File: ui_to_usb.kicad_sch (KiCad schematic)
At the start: 30 parts, among them J1 PM254-2-06-S-8.5, J2 TYPE-C-31-M-12, U3 USBLC6-2SC6, U4 CH32V305GBU6, U6 SPX3819M5-L, Y2 8M

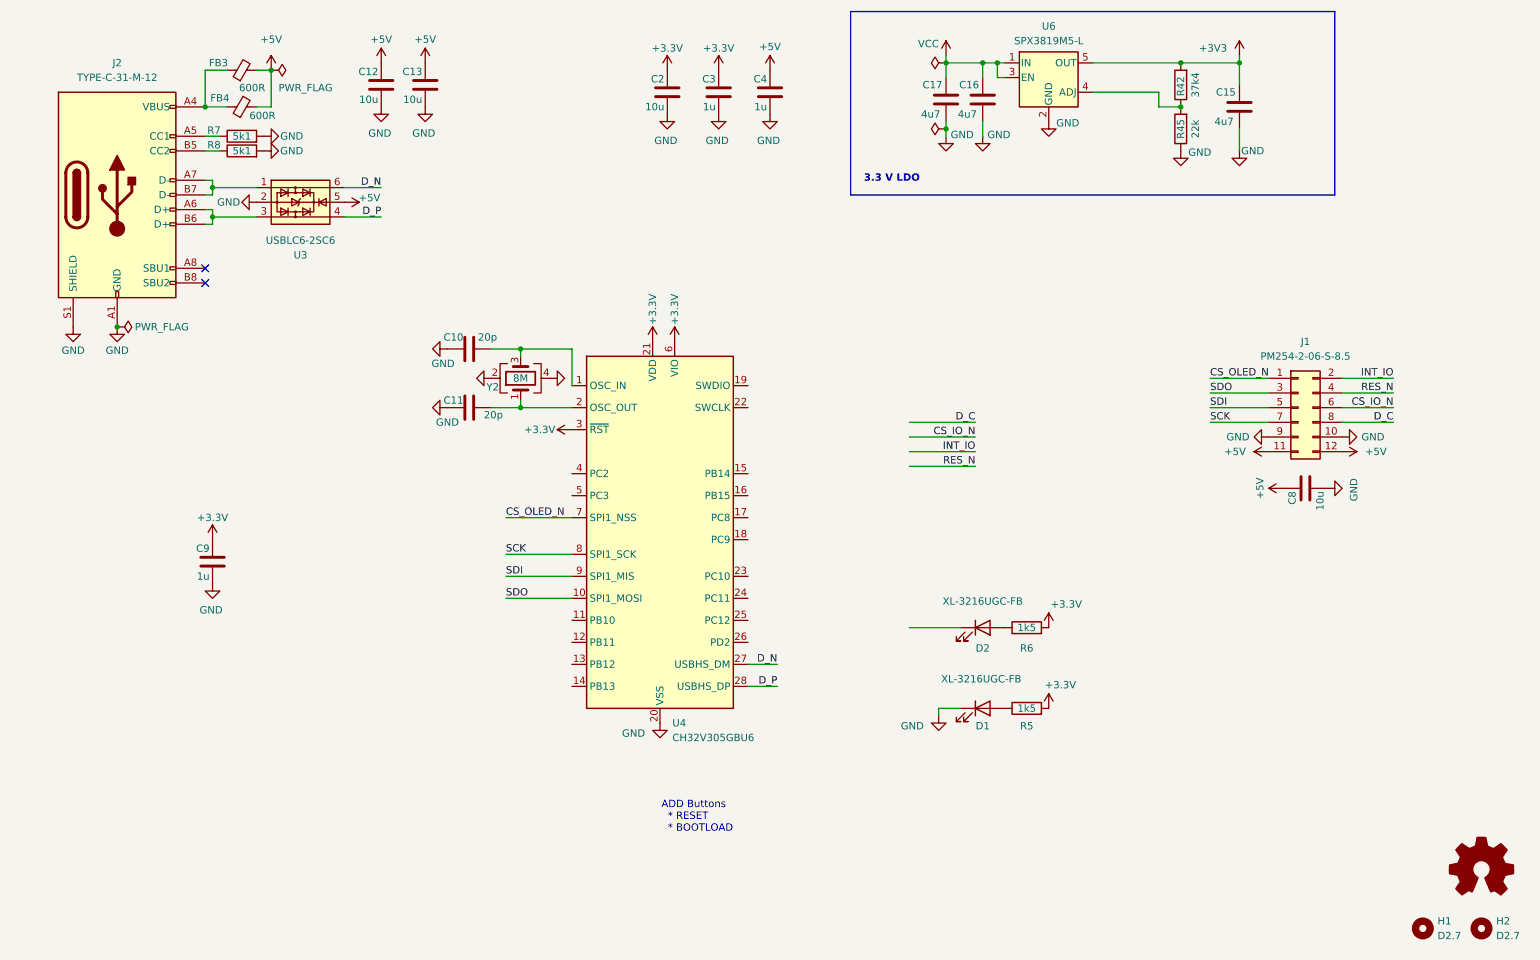
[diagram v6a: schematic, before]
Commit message: switch to CH32V203
as the V305 I've selected before doesn't have a BOOT0 pin
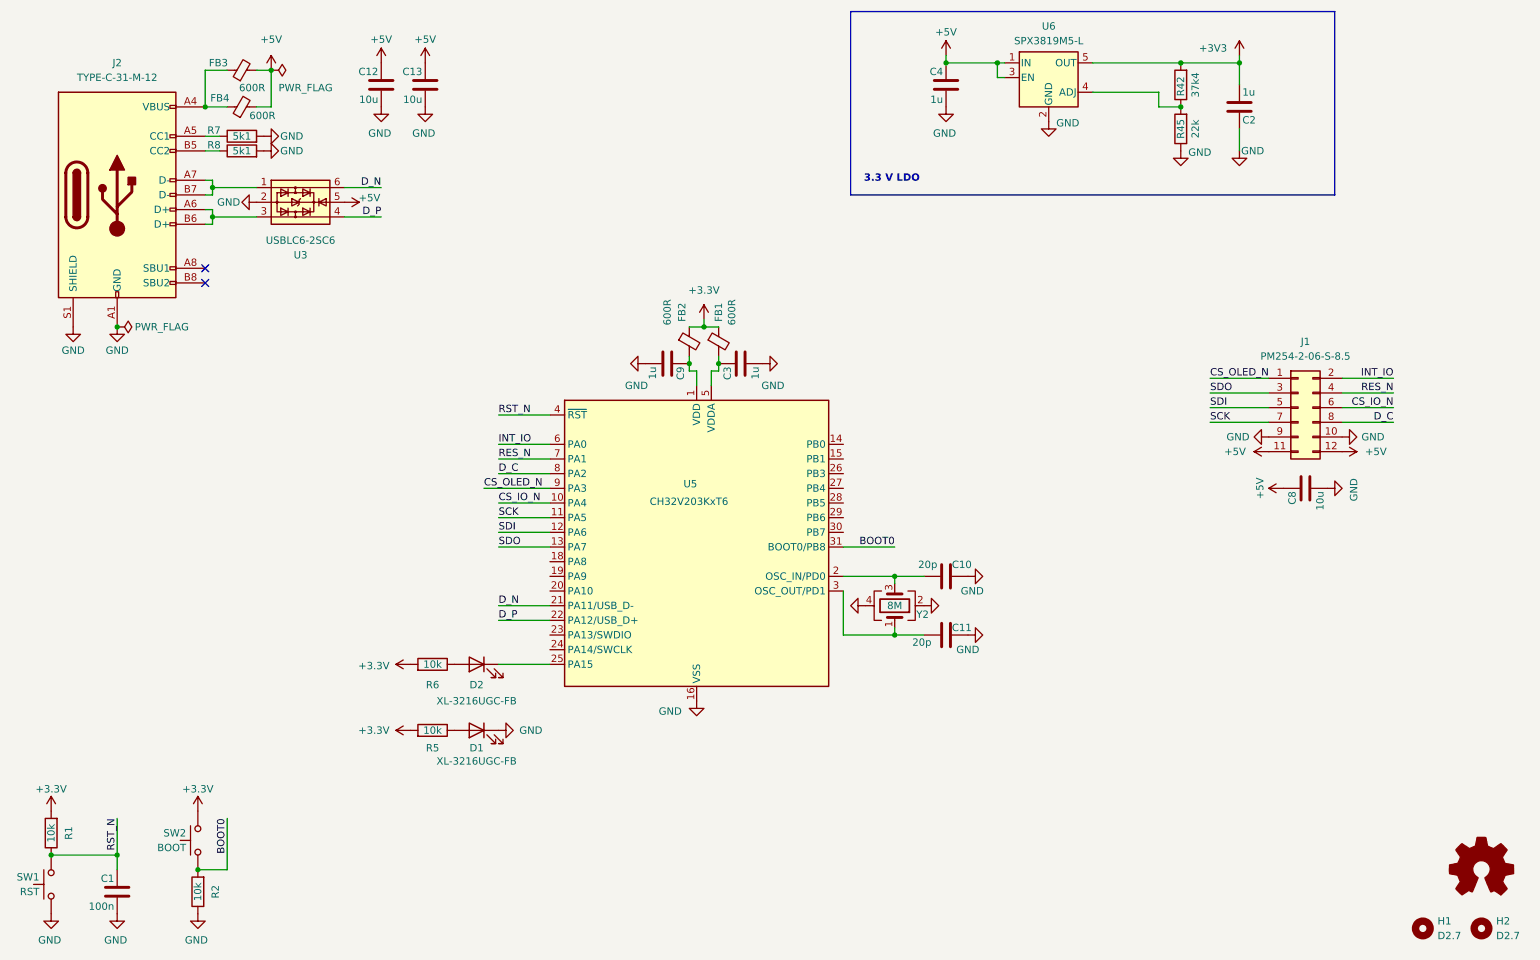
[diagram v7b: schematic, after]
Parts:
- removed C15, C16, C17: 4u7, Capacitor_SMD:C_1206_3216Metric, symbol Device:C
- removed U4: CH32V305GBU6, Package_DFN_QFN:QFN-28-1EP_4x4mm_P0.4mm_EP2.3x2.3mm, symbol lib:CH32V305GBU6
- added C1: 100n, Capacitor_SMD:C_0603_1608Metric, symbol Device:C
- added FB1, FB2: 600R, Inductor_SMD:L_0603_1608Metric, symbol Device:FerriteBead_Small
- added R1, R2: 10k, Resistor_SMD:R_0603_1608Metric, symbol Device:R
- added SW1: RST, Button_Switch_SMD:SW_SPST_B3U-3000P-B, symbol Switch:SW_Push
- added SW2: BOOT, Button_Switch_SMD:SW_SPST_B3U-3000P-B, symbol Switch:SW_Push
- added U5: CH32V203KxT6, Package_QFP:LQFP-32_7x7mm_P0.8mm, symbol lib:CH32V203KxT6
- C2: value 10u -> 1u; footprint Capacitor_SMD:C_1206_3216Metric -> Capacitor_SMD:C_0603_1608Metric
- R5, R6: value 1k5 -> 10k
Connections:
- net VCC is gone; now on net +5V: U6.1 (IN), U6.3 (EN)
- net +3.3V: now also FB1.1, FB2.1, R1.2, SW2.2; no longer C2.2, C3.2, C9.2
- net +3V3: now also C2.1
- net CS_IO_N: now also U5.10 (PA4)
- net CS_OLED_N: now also U5.9 (PA3)
- net D_C: now also U5.8 (PA2)
- net D_N: now also U5.21 (PA11/USB_D-)
- net D_P: now also U5.22 (PA12/USB_D+)
- net GND: now also C2.2, C1.1, R2.1, SW1.1, U5.16 (VSS), U5.32 (VSS); no longer C2.1
- net INT_IO: now also U5.6 (PA0)
- net RES_N: now also U5.7 (PA1)
- net SCK: now also U5.11 (PA5)
- net SDI: now also U5.12 (PA6)
- net SDO: now also U5.13 (PA7)
- net at C10.2, Y2.3: now also U5.2 (OSC_IN/PD0)
- net at C11.2, Y2.1: now also U5.3 (OSC_OUT/PD1)
- net at D2.1 (K): now also U5.25 (PA15)
- new net: C3.2, FB1.2, U5.5 (VDDA)
- new net BOOT0: R2.2, SW2.1, U5.31 (BOOT0/PB8)
- new net RST_N: C1.2, R1.1, SW1.2, U5.4 (~{RST})
- new net VDD: C9.2, FB2.2, U5.1 (VDD), U5.17 (VDD)
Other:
- note removed: "ADD Buttons * RESET * BOOTLOAD"
- moved on the sheet: C10, C11, C3, C4, C9, D1, D2, R5, R6, Y2

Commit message: schematic updates
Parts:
- U5: value CH32V203KxT6 -> CH32V203K8T6
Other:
- note added: "SPI1_MISO"
- note added: "SPI1_MOSI"
- note added: "SPI1_NSS"
- note added: "SPI1_SCK"
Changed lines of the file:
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@@
 		)
 	)
+	(text "SPI1_MISO"
+		(exclude_from_sim no)
+		(at 123.698 115.824 0)
+		(effects
+			(font
+				(size 1.27 1.27)
+			)
+			(justify left)
+		)
+	)
+	(text "SPI1_SCK"
+		(exclude_from_sim no)
+		(at 123.698 113.284 0)
+		(effects
+			(font
+				(size 1.27 1.27)
+			)
+			(justify left)
+		)
+	)
+	(text "SPI1_MOSI"
+		(exclude_from_sim no)
+		(at 123.698 118.364 0)
+		(effects
+			(font
+				(size 1.27 1.27)
+			)
+			(justify left)
+		)
+	)
+	(text "SPI1_NSS"
+		(exclude_from_sim no)
+		(at 123.698 110.744 0)
+		(effects
+			(font
+				(size 1.27 1.27)
+			)
+			(justify left)
+		)
+	)
 	(text "3.3 V LDO"
 		(exclude_from_sim no)
@@
 		(dnp no)
 		(property "Reference" "U5"
-			(at 138.684 107.188 0)
+			(at 162.306 135.382 0)
 			(effects
 				(font
 					(size 1.27 1.27)
 				)
-				(justify left)
+				(justify right)
 			)
 		)
-		(property "Value" "CH32V203KxT6"
-			(at 132.842 110.236 0)
+		(property "Value" "CH32V203K8T6"
+			(at 162.306 138.176 0)
 			(effects
 				(font
 					(size 1.27 1.27)
 				)
-				(justify left)
+				(justify right)
 			)
 		)
